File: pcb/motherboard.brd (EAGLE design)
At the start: 50.8 x 49.5 mm, 22 parts, among them U1 MIC5219 3.3V

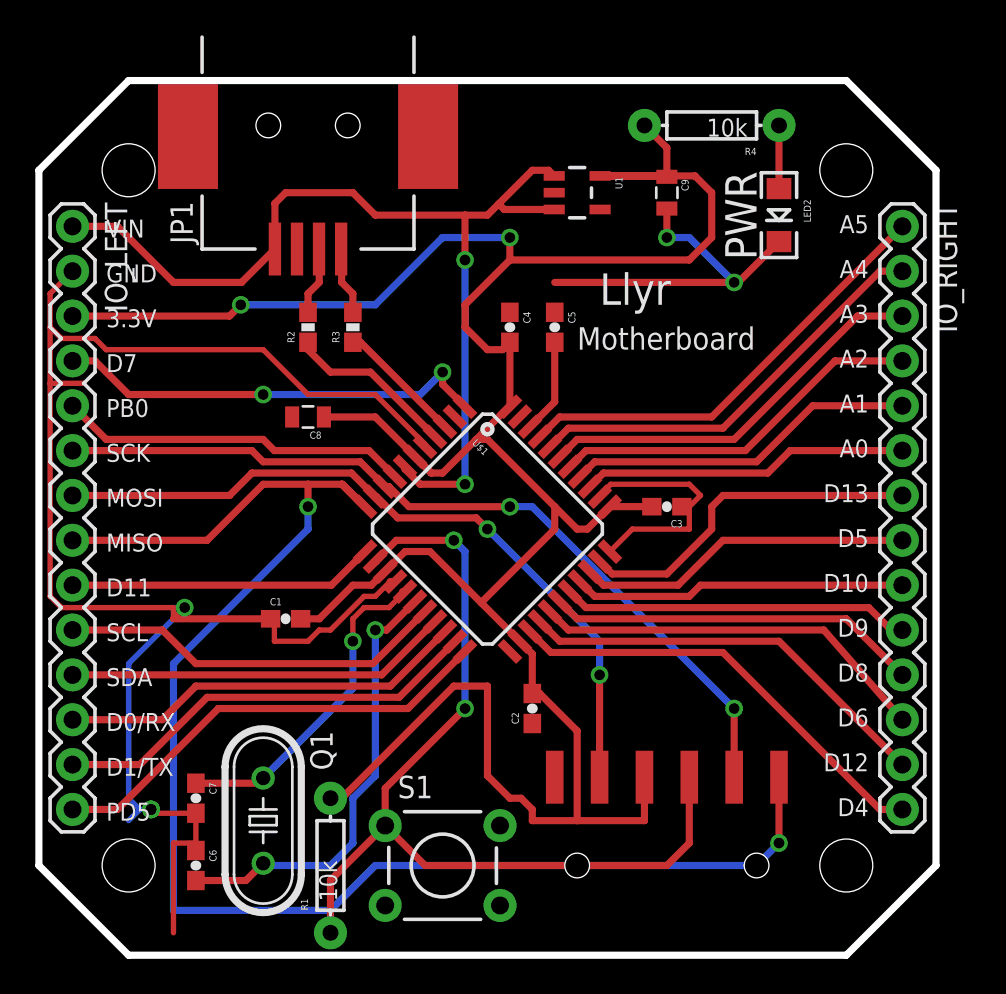
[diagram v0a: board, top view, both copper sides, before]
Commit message: - Updated PCB to include bigger components, 805 instead of 804 - Improved PCB layout
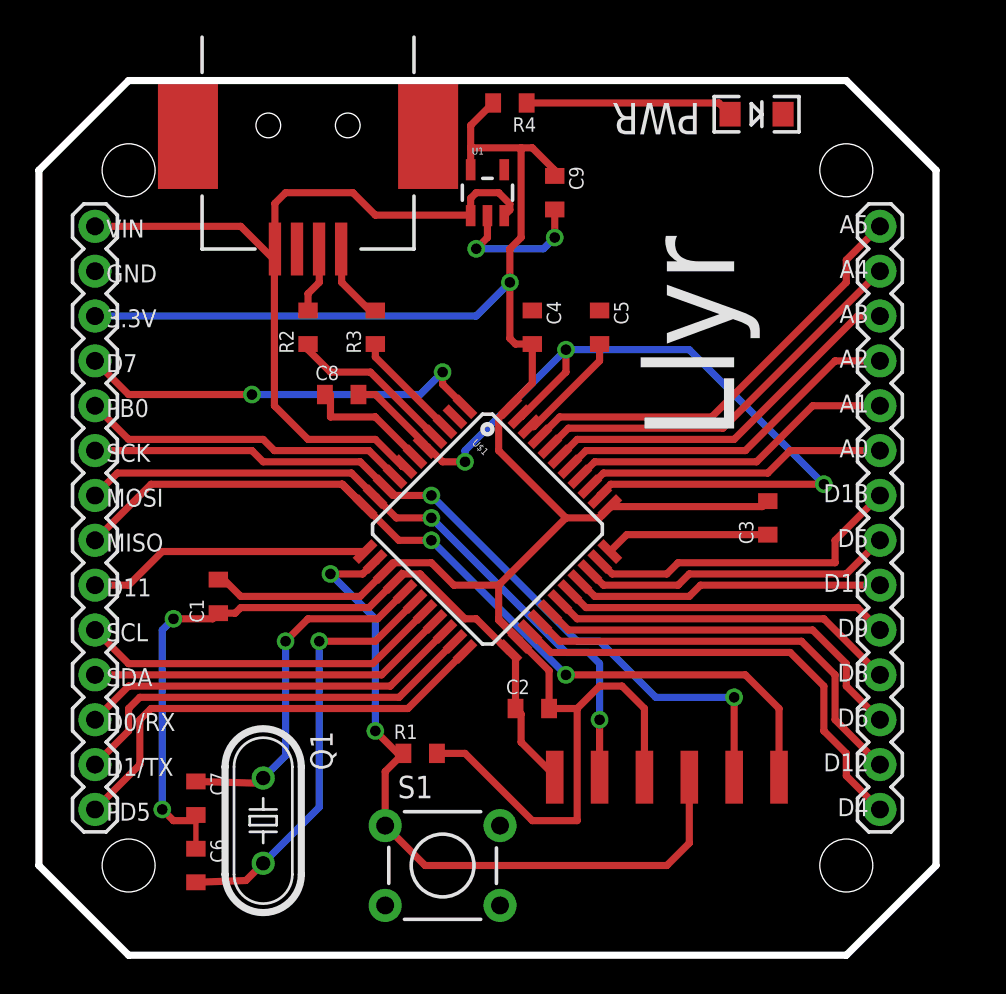
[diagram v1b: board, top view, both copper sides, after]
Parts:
- removed IO_LEFT: (no value), SparkFun-Connectors:1X14
- removed IO_RIGHT: M14, SparkFun-Connectors:1X14
- added JP2, JP3: (no value), SparkFun-Connectors:1X14
- C1, C2, C3, C4, C5, C6, C7: device SparkFun-Capacitors:0603-CAP -> ELL-i-Passives:C0805
- C8, C9: device SparkFun-Capacitors:0805 -> ELL-i-Passives:C0805
- LED2: value PWR -> (none)
- R1: device SparkFun-Resistors:AXIAL-0.3 -> ELL-i-Passives:R0805
- R2, R3: device SparkFun-Resistors:0603-RES -> ELL-i-Passives:R0805
- R4: device SparkFun-Resistors:AXIAL-0.3EZ -> ELL-i-Passives:R0805
- S1: value SWITCH-MOMENTARY-2PTH -> (none)
- moved R4 11.5 mm to (54.6, 58.4)
- moved R1 8.13 mm to (49.5, 21.6), turned to 0 degrees
- moved C9 6.35 mm to (57.1, 53.3)
- moved LED2 5.85 mm to (68.6, 57.8), turned to 0 degrees
- moved C3 5.75 mm to (69.2, 34.9), turned to 90 degrees
- moved U1 5.08 mm to (53.3, 53.3), turned to 0 degrees
- moved C1 4.02 mm to (38.1, 30.5), turned to 90 degrees
- moved C5 2.54 mm to (59.7, 45.7)
- moved C8 2.29 mm to (45.1, 41.9), turned to 0 degrees
- moved C4 1.27 mm to (55.9, 45.7)
- moved R3 1.27 mm to (47.0, 45.7)
- turned C2 to 0 degrees
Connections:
- new net N$10: C8.1, U$1.6
- net 3.3V: now also JP2.3, R1.2, R4.2; no longer C8.1, IO_LEFT.3, R1.P$2, R4.P$2, U$1.6
- net GND: now also C2.1, C3.1, JP2.2; no longer IO_LEFT.2
- net MISO: now also JP2.8; no longer IO_LEFT.8
- net MOSI: now also JP2.7; no longer IO_LEFT.7
- net N$6: now also R4.1; no longer R4.P$1
- net PB0: now also JP2.5; no longer IO_LEFT.5
- net PB4: now also JP3.11; no longer IO_RIGHT.11
- net PB5: now also JP3.10; no longer IO_RIGHT.10
- net PB6: now also JP3.9; no longer IO_RIGHT.9
- net PB7: now also JP2.9; no longer IO_LEFT.9
- net PC6: now also JP3.8; no longer IO_RIGHT.8
- net PC7: now also JP3.7; no longer IO_RIGHT.7
- net PD0: now also JP2.10; no longer IO_LEFT.10
- net PD1: now also JP2.11; no longer IO_LEFT.11
- net PD2: now also JP2.12; no longer IO_LEFT.12
- net PD3: now also JP2.13; no longer IO_LEFT.13
- net PD4: now also JP3.14; no longer IO_RIGHT.14
- net PD5: now also JP2.14; no longer IO_LEFT.14
- net PD6: now also JP3.13; no longer IO_RIGHT.13
- net PD7: now also JP3.12; no longer IO_RIGHT.12
- net PE6: now also JP2.4; no longer IO_LEFT.4
- net PF0: now also JP3.1; no longer IO_RIGHT.1
- net PF1: now also JP3.2; no longer IO_RIGHT.2
- net PF4: now also JP3.3; no longer IO_RIGHT.3
- net PF5: now also JP3.4; no longer IO_RIGHT.4
- net PF6: now also JP3.5; no longer IO_RIGHT.5
- net PF7: now also JP3.6; no longer IO_RIGHT.6
- net RESET: now also R1.1; no longer R1.P$1
- net SCK: now also JP2.6; no longer IO_LEFT.6
- net VBUS: now also JP2.1; no longer IO_LEFT.1
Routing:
- net MISO: track 87.1 -> 51.1 mm
- net 3.3V: track 159.7 -> 130.2 mm, vias 2 -> 1
- net GND: track 128.1 -> 116.1 mm, vias 4 -> 7
- net RESET: track 53.1 -> 41.9 mm
- net VBUS: track 56.3 -> 47.5 mm, vias 2 -> 0
- net N$6: track 3.58 -> 11.8 mm
- net N$10: track 0.00 -> 7.31 mm
- net MOSI: track 42.0 -> 40.1 mm
- net N$1: track 18.8 -> 20.1 mm
- net PD2: track 23.2 -> 21.9 mm
- net PD0: track 22.0 -> 20.7 mm
- net PE6: track 24.8 -> 23.5 mm
- net PD1: track 21.8 -> 20.5 mm
- net PB0: track 19.9 -> 18.7 mm
- net PF7: track 18.5 -> 17.3 mm
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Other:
- board text removed: "Motherboard"
